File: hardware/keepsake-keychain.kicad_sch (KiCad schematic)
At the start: 67 parts, among them Q1 MMFTP4042K, Q2 MMFTP4042K, Q3 MMFTP4042K, Q4 MMFTP4042K, SW1 SPDT Power Switch, SW2 PTS636 SK25J SMTR LFS, U1 74HC595 RED Shift Register, U2 74HC595 GREEN Shift Register, U3 74HC595 BLUE Shift Register, U4 Op Amp, U5 ATTINY1614, U6 MEMS Microphone

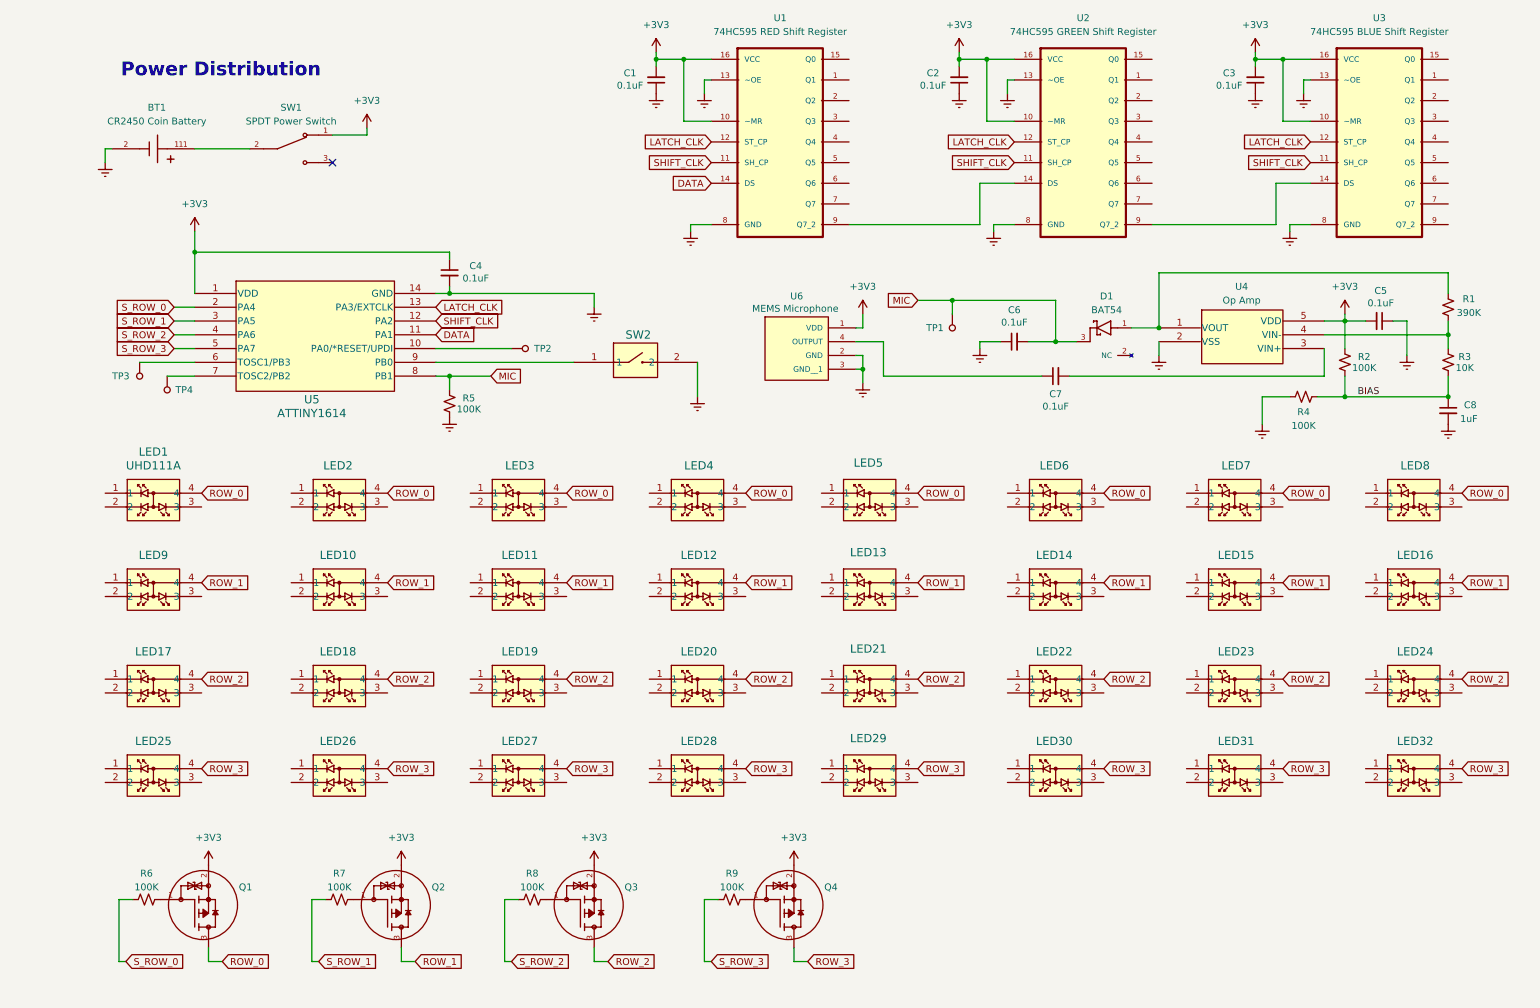
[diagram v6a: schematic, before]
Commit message: Swap push button and slide switch for better options
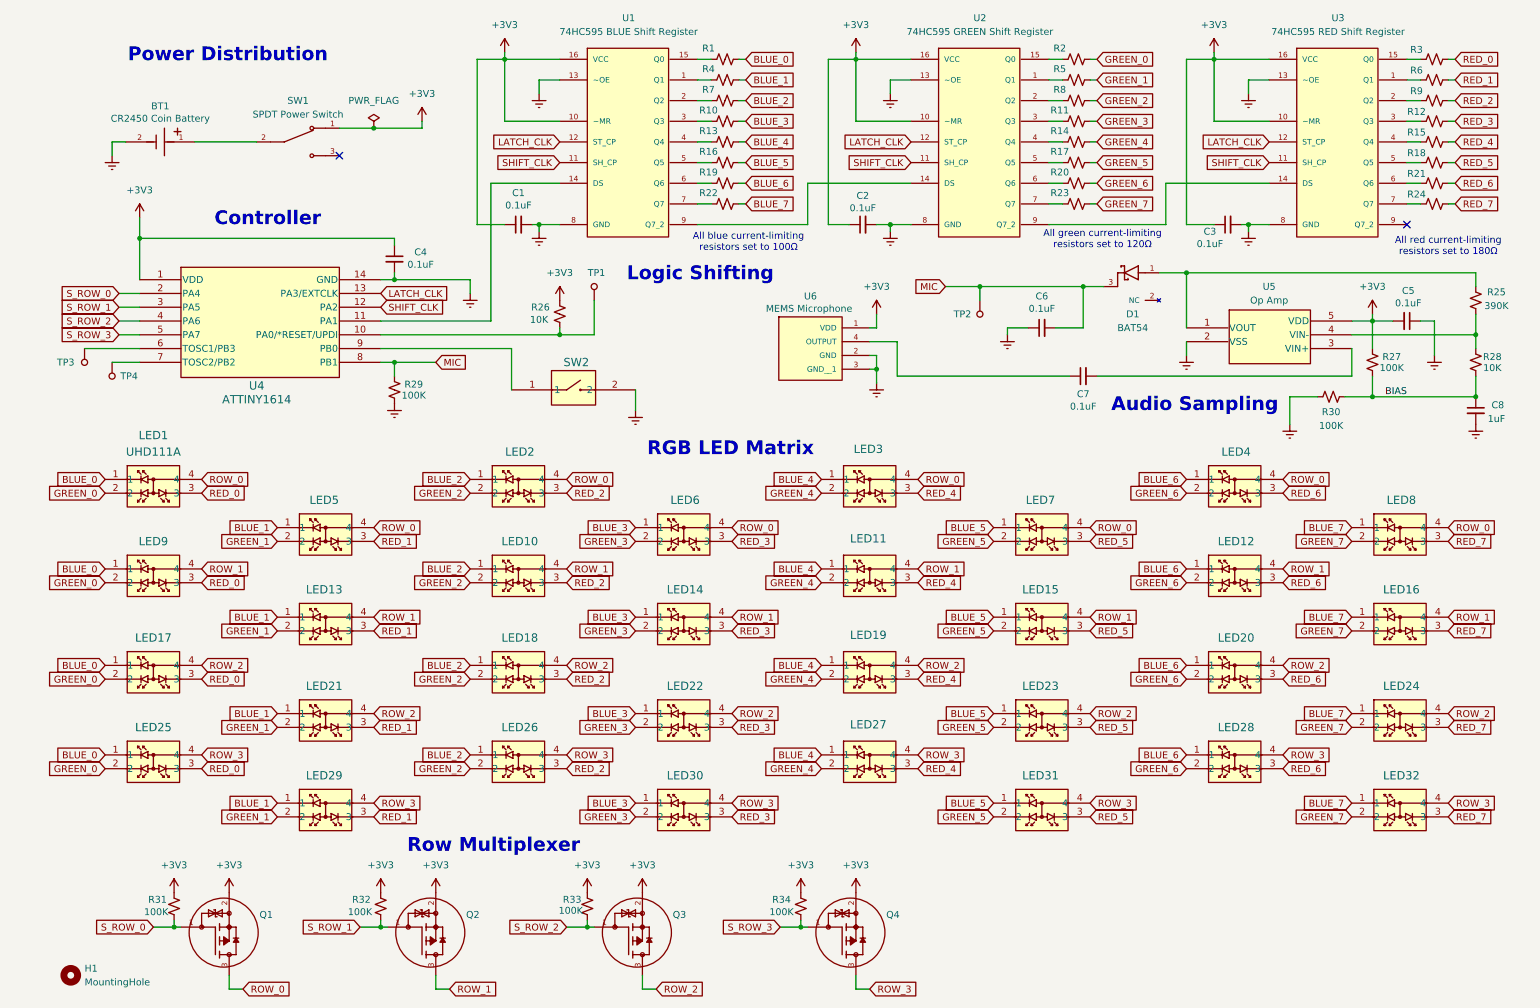
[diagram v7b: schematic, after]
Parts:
- added H1: MountingHole, MountingHole:MountingHole_3.2mm_M3_Pad_Via, symbol Mechanical:MountingHole
- added R1, R10, R13, R16, R19, R22, R4, R7: 100, Resistor_SMD:R_0603_1608Metric_Pad0.98x0.95mm_HandSolder, symbol Device:R_Small_US
- added R11, R14, R17, R2, R20, R23, R5, R8: 120, Resistor_SMD:R_0603_1608Metric_Pad0.98x0.95mm_HandSolder, symbol Device:R_Small_US
- added R12, R15, R18, R21, R24, R3, R6, R9: 180, Resistor_SMD:R_0603_1608Metric_Pad0.98x0.95mm_HandSolder, symbol Device:R_Small_US
- added R26: 10K, Resistor_SMD:R_0603_1608Metric_Pad0.98x0.95mm_HandSolder, symbol Device:R_Small_US
- BT1: footprint 0_Coin_Battery_Holder:battery-holder -> BHX1-2450-SM:BAT_BHX1-2450-SM
- D1: footprint 0_Schottky_Diode:SOT95P240X120-3N -> BAT54:SOT95P240X120-3N
- LED1, LED16, LED17, LED24, LED25, LED32, LED8, LED9: footprint 0_RGB_LED:rgb-led -> SMD4_UHD111A-FKA_CRW
- LED10: renamed from LED11; footprint 0_RGB_LED:rgb-led -> SMD4_UHD111A-FKA_CRW
- LED11: renamed from LED13; footprint 0_RGB_LED:rgb-led -> SMD4_UHD111A-FKA_CRW
- LED12: renamed from LED15; footprint 0_RGB_LED:rgb-led -> SMD4_UHD111A-FKA_CRW
- LED13: renamed from LED10; footprint 0_RGB_LED:rgb-led -> SMD4_UHD111A-FKA_CRW
- LED14: renamed from LED12; footprint 0_RGB_LED:rgb-led -> SMD4_UHD111A-FKA_CRW
- LED15: renamed from LED14; footprint 0_RGB_LED:rgb-led -> SMD4_UHD111A-FKA_CRW
- LED18: renamed from LED19; footprint 0_RGB_LED:rgb-led -> SMD4_UHD111A-FKA_CRW
- LED19: renamed from LED21; footprint 0_RGB_LED:rgb-led -> SMD4_UHD111A-FKA_CRW
- LED2: renamed from LED3; footprint 0_RGB_LED:rgb-led -> SMD4_UHD111A-FKA_CRW
- LED20: renamed from LED23; footprint 0_RGB_LED:rgb-led -> SMD4_UHD111A-FKA_CRW
- LED21: renamed from LED18; footprint 0_RGB_LED:rgb-led -> SMD4_UHD111A-FKA_CRW
- LED22: renamed from LED20; footprint 0_RGB_LED:rgb-led -> SMD4_UHD111A-FKA_CRW
- LED23: renamed from LED22; footprint 0_RGB_LED:rgb-led -> SMD4_UHD111A-FKA_CRW
- LED26: renamed from LED27; footprint 0_RGB_LED:rgb-led -> SMD4_UHD111A-FKA_CRW
- LED27: renamed from LED29; footprint 0_RGB_LED:rgb-led -> SMD4_UHD111A-FKA_CRW
- LED28: renamed from LED31; footprint 0_RGB_LED:rgb-led -> SMD4_UHD111A-FKA_CRW
- LED29: renamed from LED26; footprint 0_RGB_LED:rgb-led -> SMD4_UHD111A-FKA_CRW
- LED3: renamed from LED5; footprint 0_RGB_LED:rgb-led -> SMD4_UHD111A-FKA_CRW
- LED30: renamed from LED28; footprint 0_RGB_LED:rgb-led -> SMD4_UHD111A-FKA_CRW
- LED31: renamed from LED30; footprint 0_RGB_LED:rgb-led -> SMD4_UHD111A-FKA_CRW
- LED4: renamed from LED7; footprint 0_RGB_LED:rgb-led -> SMD4_UHD111A-FKA_CRW
- LED5: renamed from LED2; footprint 0_RGB_LED:rgb-led -> SMD4_UHD111A-FKA_CRW
- LED6: renamed from LED4; footprint 0_RGB_LED:rgb-led -> SMD4_UHD111A-FKA_CRW
- LED7: renamed from LED6; footprint 0_RGB_LED:rgb-led -> SMD4_UHD111A-FKA_CRW
- Q1, Q2, Q3, Q4: footprint 0_MOSFET:mosfet -> MMFTP4042K:TRANS_MMFTP4042K
- SW1: footprint 0_SPDT_Switch:spdt-switch -> SLW-129956-4A-RA-N-D:SW_SLW-129956-4A-RA-N-D
- SW2: footprint 0_SPDT_Switch:spdt-switch -> SW_PTS636_SK25J_SMTR_LFS_CNK
- U1: value 74HC595 RED Shift Register -> 74HC595 BLUE Shift Register; footprint 0_74HC595_Shift_Register:shift-register -> 74HC595PW_118:SOP65P640X110-16N
- U2: footprint 0_74HC595_Shift_Register:shift-register -> 74HC595PW_118:SOP65P640X110-16N
- U3: value 74HC595 BLUE Shift Register -> 74HC595 RED Shift Register; footprint 0_74HC595_Shift_Register:shift-register -> 74HC595PW_118:SOP65P640X110-16N
- U4: renamed from U5; footprint 0_ATtiny1614:SOIC14_SL_MCH -> SOIC14_SL_MCH
- U5: renamed from U4; footprint 0_Op_Amp:SOT-23-5_MC_MCH -> SOT-23-5_MC_MCH
- U6: footprint 0_Microphone:MIC_3SM123C4T1QA -> 3SM123C4T1QA:MIC_3SM123C4T1QA
- renumbered R1 to R25, R2 to R27, R3 to R28, R5 to R29, R4 to R30, R6 to R31, R7 to R32, R8 to R33, R9 to R34, TP2 to TP1, TP1 to TP2
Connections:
- net +3V3: now also C1.1, C2.1, C3.1, R31.2, R32.2, R33.2, R34.2, R26.2; no longer C1.2, C2.2, C3.2
- net GND: now also C1.2, C2.2, C3.2; no longer C1.1, C2.1, C3.1
- net S_ROW_0: now also Q1.1
- net S_ROW_1: now also Q2.1
- net S_ROW_2: now also Q3.1
- net S_ROW_3: now also Q4.1
- net at TP1.1, U4.10 (PA0/*RESET/UPDI): now also R26.1
- net BLUE_6: now reaches LED20.1
- net BLUE_6: now also LED12.1, LED28.1, LED4.1, R19.1
- net GREEN_6: now reaches LED20.2
- net GREEN_6: now also LED12.2, LED28.2, LED4.2, R20.1
- net RED_6: now reaches LED20.3
- net RED_6: now also LED12.3, LED28.3, LED4.3, R21.1
- net BLUE_7: now reaches LED32.1
- net BLUE_7: now also LED16.1, LED24.1, LED8.1, R22.1
- net GREEN_7: now reaches LED32.2
- net GREEN_7: now also LED16.2, LED24.2, LED8.2, R23.1
- net RED_7: now reaches LED32.3
- net RED_7: now also LED16.3, LED24.3, LED8.3, R24.1
- net BLUE_4: now reaches LED11.1
- net BLUE_4: now also LED19.1, LED27.1, LED3.1, R13.1
- net GREEN_4: now reaches LED11.2
- net GREEN_4: now also LED19.2, LED27.2, LED3.2, R14.1
- net RED_4: now reaches LED11.3
- net RED_4: now also LED19.3, LED27.3, LED3.3, R15.1
- net BLUE_3: now reaches LED30.1
- net BLUE_3: now also LED14.1, LED22.1, LED6.1, R10.1
- net GREEN_3: now reaches LED30.2
- net GREEN_3: now also LED14.2, LED22.2, LED6.2, R11.1
- net RED_3: now reaches LED30.3
- net RED_3: now also LED14.3, LED22.3, LED6.3, R12.1
- net BLUE_0: now reaches LED1.1
- net BLUE_0: now also LED17.1, LED25.1, LED9.1, R1.1
- net GREEN_0: now reaches LED1.2
- net GREEN_0: now also LED17.2, LED25.2, LED9.2, R2.1
- net RED_0: now reaches LED1.3
- net RED_0: now also LED17.3, LED25.3, LED9.3, R3.1
- net at U3.1 (Q1): now also R6.2
- net at U3.15 (Q0): now also R3.2
- net at U3.2 (Q2): now also R9.2
- net at U3.3 (Q3): now also R12.2
- net at U3.4 (Q4): now also R15.2
- net at U3.5 (Q5): now also R18.2
- net at U3.6 (Q6): now also R21.2
- net at U3.7 (Q7): now also R24.2
- net BLUE_5: now reaches LED23.1
- net BLUE_5: now also LED15.1, LED31.1, LED7.1, R16.1
- net GREEN_5: now reaches LED23.2
- net GREEN_5: now also LED15.2, LED31.2, LED7.2, R17.1
- net RED_5: now reaches LED23.3
- net RED_5: now also LED15.3, LED31.3, LED7.3, R18.1
- net at BT1.1, SW1.2: no longer BT1.1_1
- net BLUE_2: now reaches LED10.1
- net BLUE_2: now also LED18.1, LED2.1, LED26.1, R7.1
- net GREEN_2: now reaches LED10.2
- net GREEN_2: now also LED18.2, LED2.2, LED26.2, R8.1
- net RED_2: now reaches LED10.3
- net RED_2: now also LED18.3, LED2.3, LED26.3, R9.1
- net BLUE_1: now reaches LED21.1
- net BLUE_1: now also LED13.1, LED29.1, LED5.1, R4.1
- net GREEN_1: now reaches LED21.2
- net GREEN_1: now also LED13.2, LED29.2, LED5.2, R5.1
- net RED_1: now reaches LED21.3
- net RED_1: now also LED13.3, LED29.3, LED5.3, R6.1
- net at U1.1 (Q1): now also R4.2
- net at U1.15 (Q0): now also R1.2
- net at U1.2 (Q2): now also R7.2
- net at U1.3 (Q3): now also R10.2
- net at U1.4 (Q4): now also R13.2
- net at U1.5 (Q5): now also R16.2
- net at U1.6 (Q6): now also R19.2
- net at U1.7 (Q7): now also R22.2
- net at U2.1 (Q1): now also R5.2
- net at U2.15 (Q0): now also R2.2
- net at U2.2 (Q2): now also R8.2
- net at U2.3 (Q3): now also R11.2
- net at U2.4 (Q4): now also R14.2
- net at U2.5 (Q5): now also R17.2
- net at U2.6 (Q6): now also R20.2
- net at U2.7 (Q7): now also R23.2
- net DATA: no longer names the net of U1.14 (DS), U4.11 (PA1)
- no-connect marks 1 -> 2
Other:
- note added: "All blue current-limiting resistors set to 100Ω"
- note added: "All green current-limiting resistors set to 120Ω"
- note added: "All red current-limiting resistors set to 180Ω"
- note added: "Audio Sampling"
- note added: "Controller"
- note added: "Logic Shifting"
- note added: "RGB LED Matrix"
- note added: "Row Multiplexer"
- moved on the sheet: C1, C2, C3, C4, C5, C6, C7, C8, D1, LED1, LED10, LED11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

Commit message: Attach models. Complete schematic, pass ERC.
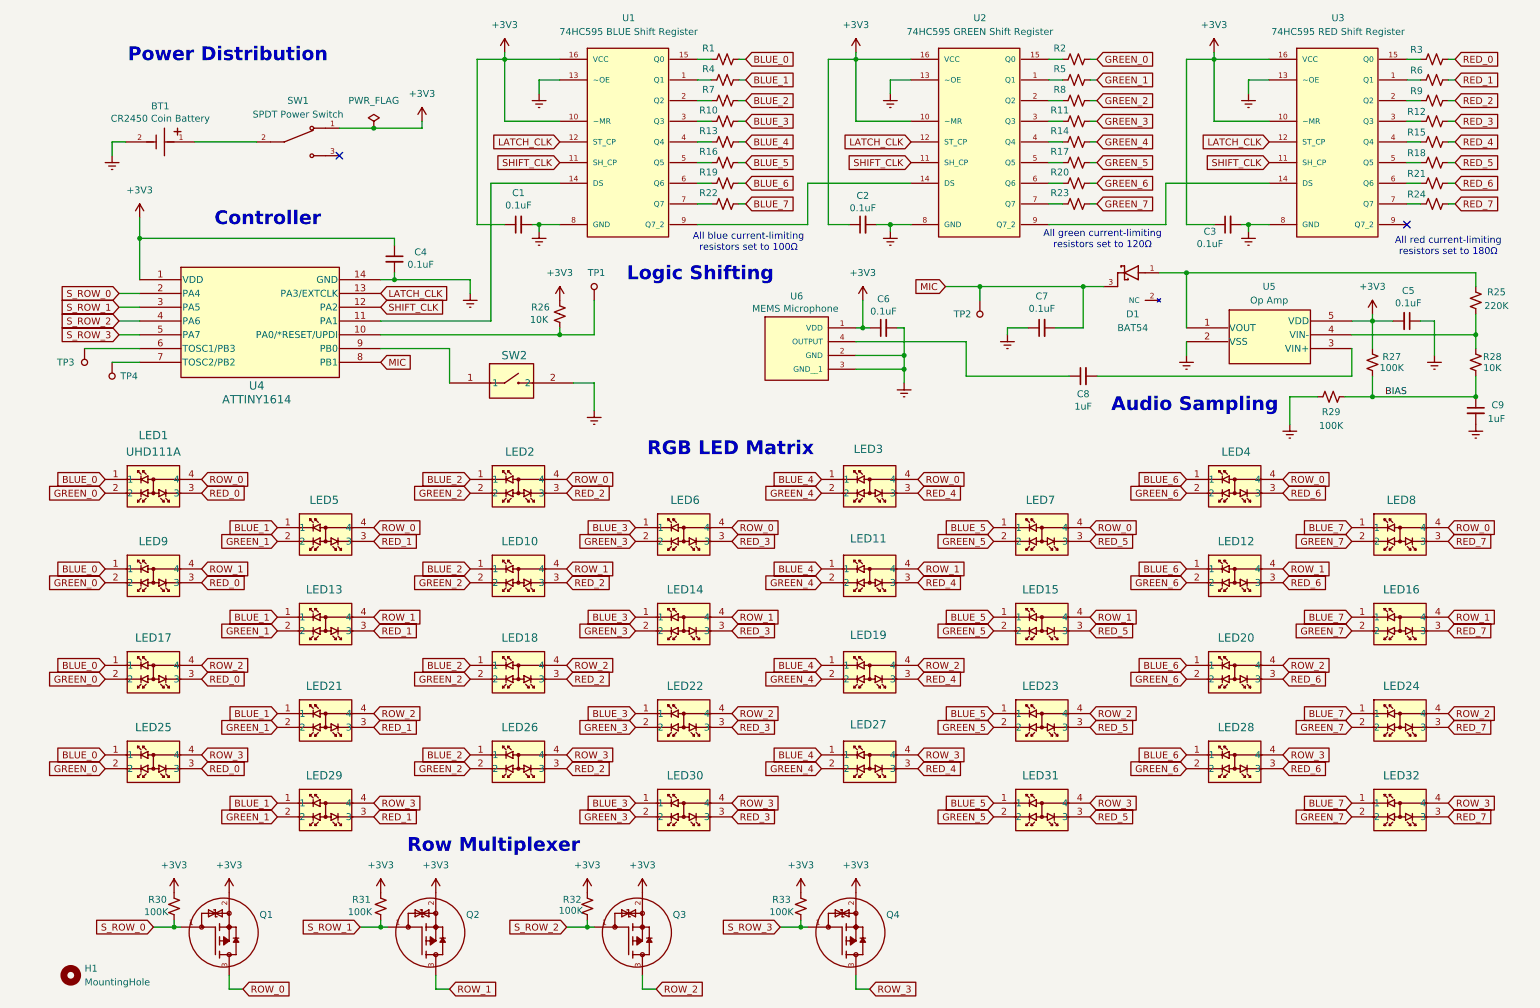
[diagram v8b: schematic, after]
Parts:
- removed R29: 100K, Resistor_SMD:R_0603_1608Metric_Pad0.98x0.95mm_HandSolder, symbol Device:R_Small_US
- added C6: 0.1uF, Capacitor_SMD:C_0603_1608Metric_Pad1.08x0.95mm_HandSolder, symbol Device:C_Small
- BT1: footprint BHX1-2450-SM:BAT_BHX1-2450-SM -> 0_Coin_Battery_Holder:battery-holder
- C8: renamed from C7; value 0.1uF -> 1uF
- D1: footprint BAT54:SOT95P240X120-3N -> 0_Schottky_Diode:SOT95P240X120-3N
- LED1, LED10, LED11, LED12, LED13, LED14, LED15, LED16, LED17, LED18, LED19, LED2, LED20, LED21, LED22, LED23, LED24, LED25, LED26, LED27, LED28, LED29, LED3, LED30, LED31, LED32, LED4, LED5, LED6, LED7, LED8, LED9: footprint SMD4_UHD111A-FKA_CRW -> 0_RGB_LED:rgb-led
- Q1, Q2, Q3, Q4: footprint MMFTP4042K:TRANS_MMFTP4042K -> 0_MOSFET:mosfet
- R25: value 390K -> 220K
- SW1: footprint SLW-129956-4A-RA-N-D:SW_SLW-129956-4A-RA-N-D -> 0_SPDT_Switch:spdt-switch
- SW2: footprint SW_PTS636_SK25J_SMTR_LFS_CNK -> 0_Tactile_Push_Button:SW_PTS636_SM43J_SMTR_LFS
- U1, U2, U3: footprint 74HC595PW_118:SOP65P640X110-16N -> 0_74HC595_Shift_Register:shift-register
- U4: footprint SOIC14_SL_MCH -> 0_ATtiny1614:SOIC14_SL_MCH
- U5: footprint SOT-23-5_MC_MCH -> 0_Op_Amp:SOT-23-5_MC_MCH
- U6: footprint 3SM123C4T1QA:MIC_3SM123C4T1QA -> 0_Microphone:MIC_3SM123C4T1QA
- renumbered C6 to C7, C8 to C9, R30 to R29, R31 to R30, R32 to R31, R33 to R32, R34 to R33
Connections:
- net +3V3: now also C6.1
- net GND: now also C6.2
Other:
- moved on the sheet: SW2, U6
